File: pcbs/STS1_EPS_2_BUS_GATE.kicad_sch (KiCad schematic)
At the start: 19 parts, among them Q5 SI7135DP-T1-GE3, Q6 2N7002, U13 4082, U3 TPS2420RSAT

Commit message: Fixed some warnings and errors.
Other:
- moved on the sheet: Q6, TP26
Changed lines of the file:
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@@
 	)
 	(junction
-		(at 168.275 128.905)
+		(at 168.91 129.54)
 		(diameter 0)
 		(color 0 0 0 0)
@@
 	(wire
 		(pts
-			(xy 143.51 39.37) (xy 160.655 39.37)
+			(xy 143.51 39.37) (xy 161.29 39.37)
 		)
 		(stroke
@@
 	(wire
 		(pts
-			(xy 78.105 54.61) (xy 76.2 54.61)
+			(xy 78.74 54.61) (xy 76.2 54.61)
 		)
 		(stroke
@@
 	(wire
 		(pts
-			(xy 160.02 134.62) (xy 160.655 134.62)
+			(xy 160.02 134.62) (xy 161.29 134.62)
 		)
 		(stroke
@@
 	(wire
 		(pts
-			(xy 168.275 124.46) (xy 168.275 128.905)
+			(xy 168.91 124.46) (xy 168.91 129.54)
 		)
 		(stroke
@@
 	(wire
 		(pts
-			(xy 78.105 57.15) (xy 76.2 57.15)
+			(xy 78.74 57.15) (xy 76.2 57.15)
 		)
 		(stroke
@@
 	(wire
 		(pts
-			(xy 168.275 139.7) (xy 168.275 147.32)
+			(xy 168.91 139.7) (xy 168.91 147.32)
 		)
 		(stroke
@@
 	(wire
 		(pts
-			(xy 168.275 128.905) (xy 168.275 129.54)
-		)
-		(stroke
-			(width 0)
-			(type default)
-		)
-	)
-	(wire
-		(pts
 			(xy 129.54 39.37) (xy 143.51 39.37)
 		)
@@
 	(text "Signal pull-ups"
 		(exclude_from_sim no)
-		(at 59.944 126.492 0)
+		(at 59.69 127 0)
 		(effects
 			(font
@@
 	(text "Gate signal logic"
 		(exclude_from_sim no)
-		(at 171.196 80.264 0)
+		(at 171.45 80.01 0)
 		(effects
 			(font
@@
 	(text "Overcurrent Protection\n"
 		(exclude_from_sim no)
-		(at 50.8 14.732 0)
+		(at 50.8 15.24 0)
 		(effects
 			(font
@@
 	(text "Bus gate FET"
 		(exclude_from_sim no)
-		(at 105.918 14.986 0)
+		(at 105.41 15.24 0)
 		(effects
 			(font
@@
 	(text "Absolute current limit: 5A\nFault current: 3,125A (corresponds to 20W @ 6,4V)\nFault timer: ~400ms to trigger, 1s to recover"
 		(exclude_from_sim no)
-		(at 38.862 115.1636 0)
+		(at 39.37 115.57 0)
 		(effects
 			(font
@@
 	(text "DT Bypass (optional)\n"
 		(exclude_from_sim no)
-		(at 106.172 27.5336 0)
+		(at 106.68 27.94 0)
 		(effects
 			(font
@@
 	(text "GATE_SIGNAL shall be pulled low,\nwhen all inhibits are released (i.e. all *_SIGNAL singals are high). \nWhen GATE_SIGNAL is pulled to GND, the bus gate opens."
 		(exclude_from_sim no)
-		(at 187.452 125.984 0)
+		(at 187.96 125.73 0)
 		(effects
 			(font
@@
 	)
 	(label "GATE_SIGNAL"
-		(at 168.275 124.46 0)
+		(at 168.91 124.46 0)
 		(fields_autoplaced yes)
 		(effects
@@
 	(hierarchical_label "VOUT_GATED"
 		(shape passive)
-		(at 160.655 39.37 0)
+		(at 161.29 39.37 0)
 		(fields_autoplaced yes)
 		(effects
@@
 	)
 	(hierarchical_label "V_INTERNAL"
-		(shape input)
+		(shape output)
 		(at 26.67 39.37 180)
 		(fields_autoplaced yes)
@@
 	(symbol
 		(lib_id "power:GND")
-		(at 78.105 54.61 90)
+		(at 78.74 54.61 90)
 		(unit 1)
 		(exclude_from_sim no)
@@
 		(fields_autoplaced yes)
 		(property "Reference" "#PWR044"
-			(at 84.455 54.61 0)
+			(at 85.09 54.61 0)
 			(effects
 				(font
@@
 		)
 		(property "Value" "GND"
-			(at 81.915 54.6099 90)
+			(at 82.55 54.6099 90)
 			(effects
 				(font
@@
 		)
 		(property "Footprint" ""
-			(at 78.105 54.61 0)
+			(at 78.74 54.61 0)
 			(effects
 				(font
@@
 		)
 		(property "Datasheet" ""
-			(at 78.105 54.61 0)
+			(at 78.74 54.61 0)
 			(effects
 				(font
@@
 			)
 		)
-		(property "Description" ""
-			(at 78.105 54.61 0)
+		(property "Description" "Power symbol creates a global label with name \"GND\" , ground"
+			(at 78.74 54.61 0)
 			(effects
 				(font
@@
 	(symbol
 		(lib_id "Transistor_FET:2N7002")
-		(at 165.735 134.62 0)
+		(at 166.37 134.62 0)
 		(unit 1)
 		(exclude_from_sim no)
@@
 		(dnp no)
 		(property "Reference" "Q6"
-			(at 172.085 139.7 0)
+			(at 172.72 139.7 0)
 			(effects
 				(font
@@
 		)
 		(property "Value" "2N7002"
-			(at 172.085 142.24 0)
+			(at 172.72 142.24 0)
 			(effects
 				(font
@@
 		)
 		(property "Footprint" "Package_TO_SOT_SMD:SOT-23"
-			(at 170.815 136.525 0)
+			(at 171.45 136.525 0)
 			(effects
 				(font
@@
 		)
 		(property "Datasheet" "https://www.onsemi.com/pub/Collateral/NDS7002A-D.PDF"
-			(at 165.735 134.62 0)
+			(at 166.37 134.62 0)
 			(effects
 				(font
@@
 			)
 		)
-		(property "Description" ""
-			(at 165.735 134.62 0)
+		(property "Description" "0.115A Id, 60V Vds, N-Channel MOSFET, SOT-23"
+			(at 166.37 134.62 0)
 			(effects
 				(font
@@
 	(symbol
 		(lib_id "Connector:TestPoint")
-		(at 168.275 128.905 270)
+		(at 168.91 129.54 270)
 		(unit 1)
 		(exclude_from_sim no)
@@
 		(fields_autoplaced yes)
 		(property "Reference" "TP26"
-			(at 173.355 127.6349 90)
+			(at 173.99 128.2699 90)
 			(effects
 				(font
@@
 		)
 		(property "Value" "TestPoint"
-			(at 173.355 130.1749 90)
+			(at 173.99 130.8099 90)
 			(effects
 				(font
@@
 		)
 		(property "Footprint" "TestPoint:TestPoint_THTPad_D1.0mm_Drill0.5mm"
-			(at 168.275 133.985 0)
+			(at 168.91 134.62 0)
 			(effects
 				(font
@@
 		)
 		(property "Datasheet" "~"
-			(at 168.275 133.985 0)
+			(at 168.91 134.62 0)
 			(effects
 				(font
@@
 		)
 		(property "Description" ""
-			(at 168.275 128.905 0)
+			(at 168.91 129.54 0)
 			(effects
 				(font
@@
 			)
 		)
-		(property "Description" ""
+		(property "Description" "Power symbol creates a global label with name \"GND\" , ground"
 			(at 143.51 53.34 0)
 			(effects
@@
 			)
 		)
-		(property "Description" ""
+		(property "Description" "Power symbol creates a global label with name \"GND\" , ground"
 			(at 71.12 102.87 0)
 			(effects
@@
 			)
 		)
-		(property "Description" ""
+		(property "Description" "Power symbol creates a global label with name \"+5V\""
 			(at 105.41 135.89 0)
 			(effects
@@
 			)
 		)
-		(property "Description" ""
+		(property "Description" "Power symbol creates a global label with name \"GND\" , ground"
 			(at 40.64 64.77 0)
 			(effects
@@
 			)
 		)
-		(property "Description" ""
+		(property "Description" "Power symbol creates a global label with name \"GND\" , ground"
 			(at 135.89 142.24 0)
 			(effects
@@
 	(symbol
 		(lib_id "power:GND")
-		(at 168.275 147.32 0)
+		(at 168.91 147.32 0)
 		(unit 1)
 		(exclude_from_sim no)
@@
 		(fields_autoplaced yes)
 		(property "Reference" "#PWR0107"
-			(at 168.275 153.67 0)
+			(at 168.91 153.67 0)
 			(effects
 				(font
@@
 		)
 		(property "Value" "GND"
-			(at 168.275 152.4 0)
+			(at 168.91 152.4 0)
 			(effects
 				(font
@@
 		)
 		(property "Footprint" ""
-			(at 168.275 147.32 0)
+			(at 168.91 147.32 0)
 			(effects
 				(font
@@
 		)
 		(property "Datasheet" ""
-			(at 168.275 147.32 0)
+			(at 168.91 147.32 0)
 			(effects
 				(font
@@
 			)
 		)
-		(property "Description" ""
-			(at 168.275 147.32 0)
+		(property "Description" "Power symbol creates a global label with name \"GND\" , ground"
+			(at 168.91 147.32 0)
 			(effects
 				(font
@@
 			)
 		)
-		(property "Description" ""
+		(property "Description" "Power symbol creates a global label with name \"GND\" , ground"
 			(at 135.89 104.14 0)
 			(effects
@@
 			)
 		)
-		(property "Description" ""
+		(property "Description" "Power symbol creates a global label with name \"GND\" , ground"
 			(at 43.18 102.87 0)
 			(effects
@@
 			)
 		)
-		(property "Description" ""
+		(property "Description" "Power symbol creates a global label with name \"GND\" , ground"
 			(at 60.96 102.87 0)
 			(effects
@@
 	(symbol
 		(lib_id "power:GND")
-		(at 78.105 57.15 90)
+		(at 78.74 57.15 90)
 		(unit 1)
 		(exclude_from_sim no)
@@
 		(fields_autoplaced yes)
 		(property "Reference" "#PWR045"
-			(at 84.455 57.15 0)
+			(at 85.09 57.15 0)
 			(effects
 				(font
@@
 		)
 		(property "Value" "GND"
-			(at 81.915 57.1499 90)
+			(at 82.55 57.1499 90)
 			(effects
 				(font
@@
 		)
 		(property "Footprint" ""
-			(at 78.105 57.15 0)
+			(at 78.74 57.15 0)
 			(effects
 				(font
@@
 		)
 		(property "Datasheet" ""
-			(at 78.105 57.15 0)
+			(at 78.74 57.15 0)
 			(effects
 				(font
@@
 			)
 		)
-		(property "Description" ""
-			(at 78.105 57.15 0)
+		(property "Description" "Power symbol creates a global label with name \"GND\" , ground"
+			(at 78.74 57.15 0)
 			(effects
 				(font
@@
 			)
 		)
-		(property "Description" ""
+		(property "Description" "Power symbol creates a global label with name \"GND\" , ground"
 			(at 40.64 52.07 0)
 			(effects
@@
 			)
 		)
-		(property "Description" ""
+		(property "Description" "Power symbol creates a global label with name \"GND\" , ground"
 			(at 40.64 59.69 0)
 			(effects
@@
 			)
 		)
-		(property "Description" ""
+		(property "Description" "Power symbol creates a global label with name \"GND\" , ground"
 			(at 52.07 102.87 0)
 			(effects
@@
 			)
 		)
-		(property "Description" ""
+		(property "Description" "Power symbol creates a global label with name \"GND\" , ground"
 			(at 40.64 69.85 0)
 			(effects

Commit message: Fixed warnings and errors.
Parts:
- U3: footprint STS_Package_DFN_QFN:QFN65P400X400X100-17N -> Package_DFN_QFN:VQFN-16-1EP_3x3mm_P0.5mm_EP1.45x1.45mm_ThermalVias
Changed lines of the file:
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@@
 			)
 		)
-		(property "Footprint" "STS_Package_DFN_QFN:QFN65P400X400X100-17N"
+		(property "Footprint" "Package_DFN_QFN:VQFN-16-1EP_3x3mm_P0.5mm_EP1.45x1.45mm_ThermalVias"
 			(at 58.42 52.07 0)
 			(effects

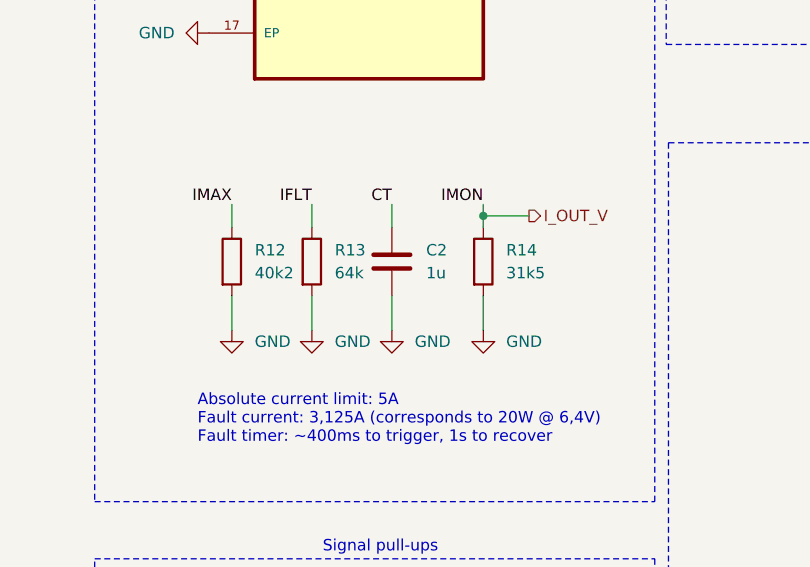
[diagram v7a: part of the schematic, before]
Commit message: Modified some resistor values slightly, so that they fall in common resistor series.
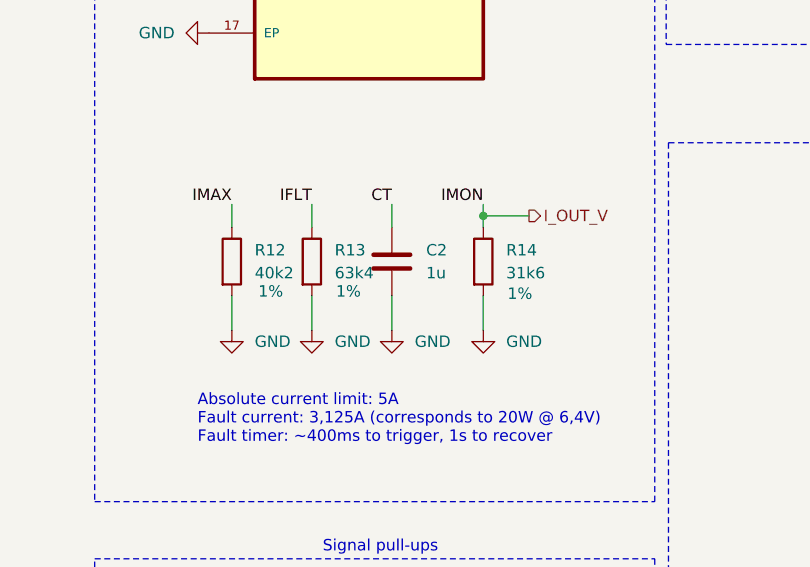
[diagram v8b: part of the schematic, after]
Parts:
- R12: Tolerance (none) -> 1%
- R13: value 64k -> 63k4; Tolerance (none) -> 1%
- R14: value 31k5 -> 31k6; Tolerance (none) -> 1%
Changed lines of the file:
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@@
 		(on_board yes)
 		(dnp no)
-		(fields_autoplaced yes)
 		(property "Reference" "R12"
 			(at 45.72 93.9799 0)
@@
 				)
 				(hide yes)
+			)
+		)
+		(property "Tolerance" "1%"
+			(at 47.498 98.552 0)
+			(effects
+				(font
+					(size 1.27 1.27)
+				)
 			)
 		)
@@
 		(on_board yes)
 		(dnp no)
-		(fields_autoplaced yes)
 		(property "Reference" "R13"
 			(at 54.61 93.9799 0)
@@
 			)
 		)
-		(property "Value" "64k"
+		(property "Value" "63k4"
 			(at 54.61 96.5199 0)
 			(effects
@@
 				)
 				(hide yes)
+			)
+		)
+		(property "Tolerance" "1%"
+			(at 56.134 98.552 0)
+			(effects
+				(font
+					(size 1.27 1.27)
+				)
 			)
 		)
@@
 		(on_board yes)
 		(dnp no)
-		(fields_autoplaced yes)
 		(property "Reference" "R14"
 			(at 73.66 93.9799 0)
@@
 			)
 		)
-		(property "Value" "31k5"
+		(property "Value" "31k6"
 			(at 73.66 96.5199 0)
 			(effects
@@
 			)
 		)
+		(property "Tolerance" "1%"
+			(at 75.184 98.806 0)
+			(effects
+				(font
+					(size 1.27 1.27)
+				)
+			)
+		)
